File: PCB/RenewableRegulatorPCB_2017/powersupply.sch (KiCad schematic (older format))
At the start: 12 parts, among them U2 LMR16006, U3 MCP1702-50

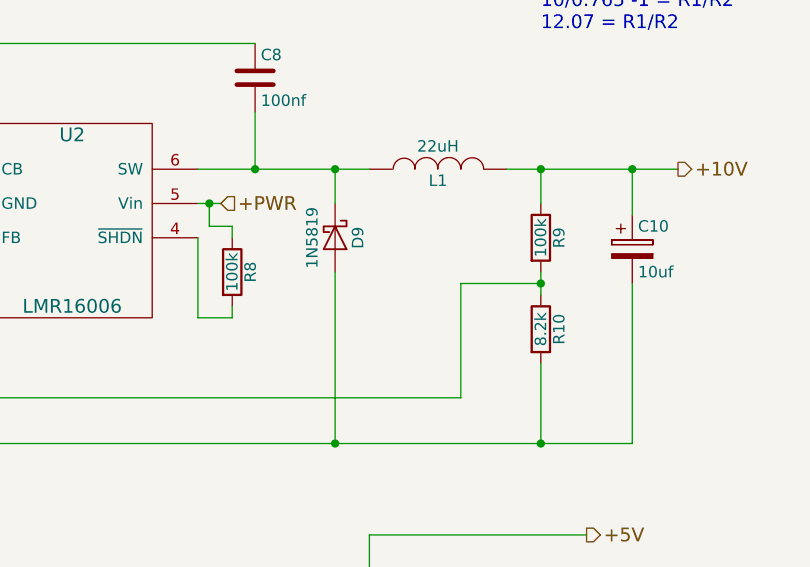
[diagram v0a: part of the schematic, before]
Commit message: Moved code into new file structure
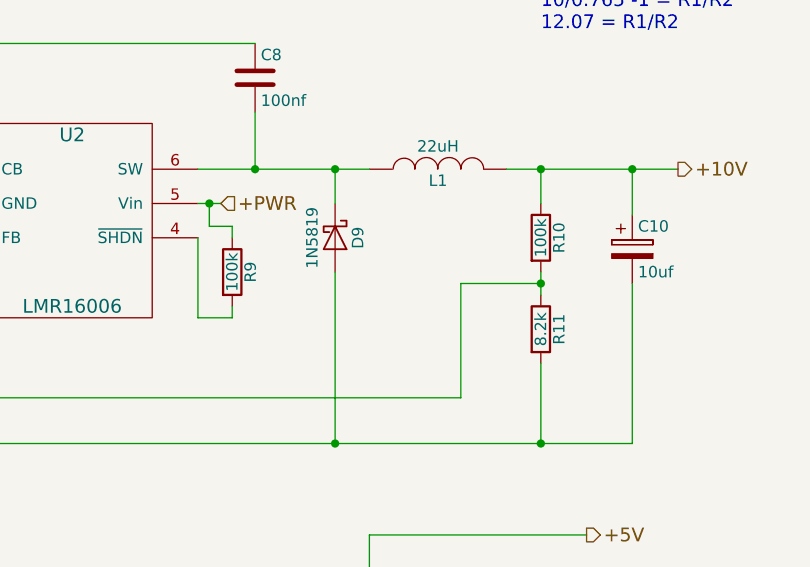
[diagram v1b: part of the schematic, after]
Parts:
- renumbered R9 to R10, R10 to R11, R8 to R9
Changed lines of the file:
@@
 $EndComp
 $Comp
-L R R9
+L R R10
 U 1 1 58E394A9
 P 6300 3500
-F 0 "R9" V 6380 3500 50  0000 C CNN
+F 0 "R10" V 6380 3500 50  0000 C CNN
 F 1 "100k" V 6300 3500 50  0000 C CNN
 F 2 "REInnovationFootprint:TH_Resistor_1" V 6230 3500 50  0001 C CNN
@@
 $EndComp
 $Comp
-L R R10
+L R R11
 U 1 1 58E394EA
 P 6300 3900
-F 0 "R10" V 6380 3900 50  0000 C CNN
+F 0 "R11" V 6380 3900 50  0000 C CNN
 F 1 "8.2k" V 6300 3900 50  0000 C CNN
 F 2 "REInnovationFootprint:TH_Resistor_1" V 6230 3900 50  0001 C CNN
@@
 VOUT = 0.765 V (1+(R1/R2))\n10/0.765 -1 = R1/R2\n12.07 = R1/R2
 $Comp
-L R R8
+L R R9
 U 1 1 58E3B2B4
 P 4950 3650
-F 0 "R8" V 5030 3650 50  0000 C CNN
+F 0 "R9" V 5030 3650 50  0000 C CNN
 F 1 "100k" V 4950 3650 50  0000 C CNN
 F 2 "REInnovationFootprint:TH_Resistor_1" V 4880 3650 50  0001 C CNN

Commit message: Large update of PCB design
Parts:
- added P11: TP_GND, matts_components:1pin_0_8mm, symbol CONN_01X01
- added P12: TP_5V, matts_components:1pin_0_8mm, symbol CONN_01X01
- added P13: TP_10V, matts_components:1pin_0_8mm, symbol CONN_01X01
- C10: Description Low ESR -> Low ESR. 25V; Manufacturer (none) -> Panasonic; Manufacturer Part No (none) -> EEUFR1H100; Supplier 1 (none) -> RS; Supplier 1 Cost (none) -> 0.047; Supplier 1 Part No (none) -> 923-2745
- C6: Description 60V+ Ceramic -> 60V+ Ceramic Low ESR; Manufacturer (none) -> Murata; Manufacturer Part No (none) -> RDEC72A225K3M1H03A; Supplier 1 (none) -> RS; Supplier 1 Cost (none) -> 0.79; Supplier 1 Part No (none) -> 133-5714
- C7, C9: Description (none) -> >25V Electrolytic/Ceramic; Manufacturer (none) -> Murata; Manufacturer Part No (none) -> RCER71H105K2M1H03A; Supplier 1 (none) -> RS; Supplier 1 Cost (none) -> 0.28; Supplier 1 Part No (none) -> 841-0755
- U2: footprint matts_components:SOT23-5_matt -> REInnovationFootprint:SM_SOT23-6
- U3: Description (none) -> LDO 5V supply. 250mA; Manufacturer (none) -> MicroChip; Manufacturer Part No (none) -> MCP1702-5002E/TO; Supplier 1 (none) -> RS; Supplier 1 Cost (none) -> 0.358; Supplier 1 Part No (none) -> 403-856
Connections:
- net +10V: now also P13.1 (P1)
- net +5V: now also P12.1 (P1)
- net GND: now also P11.1 (P1)
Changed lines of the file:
@@
 F 2 "REInnovationFootprint:C_1V7_TH" H 4400 5450 60  0001 C CNN
 F 3 "" H 4400 5450 60  0001 C CNN
+F 4 "~" H 4400 5450 60  0000 C CNN "Notes"
+F 5 ">25V Electrolytic/Ceramic" H 4400 5450 60  0001 C CNN "Description"
+F 6 "Murata" H 4400 5450 60  0001 C CNN "Manufacturer"
+F 7 "RCER71H105K2M1H03A" H 4400 5450 60  0001 C CNN "Manufacturer Part No"
+F 8 "RS" H 4400 5450 60  0001 C CNN "Supplier 1"
+F 9 "841-0755" H 4400 5450 60  0001 C CNN "Supplier 1 Part No"
+F 10 "0.28" H 4400 5450 60  0001 C CNN "Supplier 1 Cost"
+F 11 "~" H 4400 5450 60  0001 C CNN "Supplier 2"
+F 12 "~" H 4400 5450 60  0001 C CNN "Supplier 2 Part No"
+F 13 "~" H 4400 5450 60  0001 C CNN "Supplier 2 Cost"
 	1    4400 5450
-	1    0    0    -1
-$EndComp
-$Comp
-L CP1-RESCUE-RenewableRegulatorPCB_2017 C9
-U 1 1 50D36323
-P 5550 5500
-F 0 "C9" H 5600 5600 50  0000 L CNN
-F 1 "1uf" H 5600 5400 50  0000 L CNN
-F 2 "REInnovationFootprint:C_1V7_TH" H 5550 5500 60  0001 C CNN
-F 3 "" H 5550 5500 60  0001 C CNN
-	1    5550 5500
 	1    0    0    -1
 $EndComp
@@
 +5V
 Wire Wire Line
-	5550 5950 2600 5950
+	2600 5950 5750 5950
 Connection ~ 4900 5950
 Connection ~ 4400 5950
@@
 F 0 "U2" H 4250 3750 60  0000 C CNN
 F 1 "LMR16006" H 4250 3000 60  0000 C CNN
-F 2 "matts_components:SOT23-5_matt" H 4800 3500 60  0001 C CNN
+F 2 "REInnovationFootprint:SM_SOT23-6" H 4800 3500 60  0001 C CNN
 F 3 "http://www.ti.com/lit/ds/symlink/lmr16006.pdf" H 4800 3500 60  0001 C CNN
 F 4 "~" H 4250 3400 60  0000 C CNN "Notes"
@@
 F 1 "2.2uf" H 2875 3100 50  0000 L CNN
 F 2 "REInnovationFootprint:C_1V7_TH" H 2888 3050 50  0001 C CNN
-F 3 "" H 2850 3200 50  0000 C CNN
+F 3 "http://docs-europe.electrocomponents.com/webdocs/156e/0900766b8156ecdd.pdf" H 2850 3200 50  0001 C CNN
 F 4 "~" H 2850 3200 60  0000 C CNN "Notes"
-F 5 "60V+ Ceramic" H 2850 3200 60  0001 C CNN "Description"
-F 6 "~" H 2850 3200 60  0001 C CNN "Manufacturer"
-F 7 "~" H 2850 3200 60  0001 C CNN "Manufacturer Part No"
-F 8 "~" H 2850 3200 60  0001 C CNN "Supplier 1"
-F 9 "~" H 2850 3200 60  0001 C CNN "Supplier 1 Part No"
-F 10 "~" H 2850 3200 60  0001 C CNN "Supplier 1 Cost"
+F 5 "60V+ Ceramic Low ESR" H 2850 3200 60  0001 C CNN "Description"
+F 6 "Murata" H 2850 3200 60  0001 C CNN "Manufacturer"
+F 7 "RDEC72A225K3M1H03A" H 2850 3200 60  0001 C CNN "Manufacturer Part No"
+F 8 "RS" H 2850 3200 60  0001 C CNN "Supplier 1"
+F 9 "133-5714" H 2850 3200 60  0001 C CNN "Supplier 1 Part No"
+F 10 "0.79" H 2850 3200 60  0001 C CNN "Supplier 1 Cost"
 F 11 "~" H 2850 3200 60  0001 C CNN "Supplier 2"
 F 12 "~" H 2850 3200 60  0001 C CNN "Supplier 2 Part No"
@@
 F 3 "http://docs-europe.electrocomponents.com/webdocs/0a77/0900766b80a77df4.pdf" H 4900 5250 60  0001 C CNN
 F 4 "~" H 4900 5250 60  0000 C CNN "Notes"
-F 5 "~" H 4900 5250 60  0001 C CNN "Description"
-F 6 "~" H 4900 5250 60  0001 C CNN "Manufacturer"
-F 7 "~" H 4900 5250 60  0001 C CNN "Manufacturer Part No"
-F 8 "~" H 4900 5250 60  0001 C CNN "Supplier 1"
-F 9 "~" H 4900 5250 60  0001 C CNN "Supplier 1 Part No"
-F 10 "~" H 4900 5250 60  0001 C CNN "Supplier 1 Cost"
+F 5 "LDO 5V supply. 250mA" H 4900 5250 60  0001 C CNN "Description"
+F 6 "MicroChip" H 4900 5250 60  0001 C CNN "Manufacturer"
+F 7 "MCP1702-5002E/TO" H 4900 5250 60  0001 C CNN "Manufacturer Part No"
+F 8 "RS" H 4900 5250 60  0001 C CNN "Supplier 1"
+F 9 "403-856" H 4900 5250 60  0001 C CNN "Supplier 1 Part No"
+F 10 "0.358" H 4900 5250 60  0001 C CNN "Supplier 1 Cost"
 F 11 "~" H 4900 5250 60  0001 C CNN "Supplier 2"
 F 12 "~" H 4900 5250 60  0001 C CNN "Supplier 2 Part No"
@@
 F 3 "" H 6700 3550 50  0000 C CNN
 F 4 "~" H 6700 3550 60  0000 C CNN "Notes"
-F 5 "Low ESR" H 6700 3550 60  0001 C CNN "Description"
-F 6 "~" H 6700 3550 60  0001 C CNN "Manufacturer"
-F 7 "~" H 6700 3550 60  0001 C CNN "Manufacturer Part No"
-F 8 "~" H 6700 3550 60  0001 C CNN "Supplier 1"
-F 9 "~" H 6700 3550 60  0001 C CNN "Supplier 1 Part No"
-F 10 "~" H 6700 3550 60  0001 C CNN "Supplier 1 Cost"
+F 5 "Low ESR. 25V" H 6700 3550 60  0001 C CNN "Description"
+F 6 "Panasonic" H 6700 3550 60  0001 C CNN "Manufacturer"
+F 7 "EEUFR1H100" H 6700 3550 60  0001 C CNN "Manufacturer Part No"
+F 8 "RS" H 6700 3550 60  0001 C CNN "Supplier 1"
+F 9 "923-2745" H 6700 3550 60  0001 C CNN "Supplier 1 Part No"
+F 10 "0.047" H 6700 3550 60  0001 C CNN "Supplier 1 Cost"
 F 11 "~" H 6700 3550 60  0001 C CNN "Supplier 2"
 F 12 "~" H 6700 3550 60  0001 C CNN "Supplier 2 Part No"
@@
 Wire Wire Line
 	2850 2900 2650 2900
+$Comp
+L CONN_01X01 P13
+U 1 1 58E51FB7
+P 6750 2950
+F 0 "P13" H 6750 3050 50  0000 C CNN
+F 1 "TP_10V" V 6850 2950 50  0000 C CNN
+F 2 "matts_components:1pin_0_8mm" H 6750 2950 50  0001 C CNN
+F 3 "" H 6750 2950 50  0000 C CNN
+	1    6750 2950
+	1    0    0    -1
+$EndComp
+$Comp
+L CONN_01X01 P12
+U 1 1 58E5205A
+P 6300 5050
+F 0 "P12" H 6300 5150 50  0000 C CNN
+F 1 "TP_5V" V 6400 5050 50  0000 C CNN
+F 2 "matts_components:1pin_0_8mm" H 6300 5050 50  0001 C CNN
+F 3 "" H 6300 5050 50  0000 C CNN
+	1    6300 5050
+	1    0    0    -1
+$EndComp
+$Comp
+L CONN_01X01 P11
+U 1 1 58E520E9
+P 5950 5950
+F 0 "P11" H 5950 6050 50  0000 C CNN
+F 1 "TP_GND" V 6050 5950 50  0000 C CNN
+F 2 "matts_components:1pin_0_8mm" H 5950 5950 50  0001 C CNN
+F 3 "" H 5950 5950 50  0000 C CNN
+	1    5950 5950
+	1    0    0    -1
+$EndComp
+Wire Wire Line
+	6550 2950 6450 2950
+Wire Wire Line
+	6450 2950 6450 3200
+Connection ~ 6450 3200
+Wire Wire Line
+	6100 5050 5950 5050
+Wire Wire Line
+	5950 5050 5950 4800
+Connection ~ 5950 4800
+Connection ~ 5550 5950
+$Comp
+L CP1-RESCUE-RenewableRegulatorPCB_2017 C9
+U 1 1 58E5783F
+P 5550 5500
+F 0 "C9" H 5600 5600 50  0000 L CNN
+F 1 "1uf" H 5600 5400 50  0000 L CNN
+F 2 "REInnovationFootprint:C_1V7_TH" H 5550 5500 60  0001 C CNN
+F 3 "" H 5550 5500 60  0001 C CNN
+F 4 "~" H 5550 5500 60  0000 C CNN "Notes"
+F 5 ">25V Electrolytic/Ceramic" H 5550 5500 60  0001 C CNN "Description"
+F 6 "Murata" H 5550 5500 60  0001 C CNN "Manufacturer"
+F 7 "RCER71H105K2M1H03A" H 5550 5500 60  0001 C CNN "Manufacturer Part No"
+F 8 "RS" H 5550 5500 60  0001 C CNN "Supplier 1"
+F 9 "841-0755" H 5550 5500 60  0001 C CNN "Supplier 1 Part No"
+F 10 "0.28" H 5550 5500 60  0001 C CNN "Supplier 1 Cost"
+F 11 "~" H 5550 5500 60  0001 C CNN "Supplier 2"
+F 12 "~" H 5550 5500 60  0001 C CNN "Supplier 2 Part No"
+F 13 "~" H 5550 5500 60  0001 C CNN "Supplier 2 Cost"
+	1    5550 5500
+	1    0    0    -1
+$EndComp
 $EndSCHEMATC

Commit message: Secod
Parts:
- C10: footprint REInnovationFootprint:C_1V7_TH -> RenewableRegulatorPCB_2017_Library_Yoan:Capacitor_C10_1V7_TH
- C6: footprint REInnovationFootprint:C_1V7_TH -> RenewableRegulatorPCB_2017_Library_Yoan:Capacitor_C6_1V7_TH
- C7: footprint REInnovationFootprint:C_1V7_TH -> RenewableRegulatorPCB_2017_Library_Yoan:Capacitor_C7_1V7_TH
- C9: footprint REInnovationFootprint:C_1V7_TH -> RenewableRegulatorPCB_2017_Library_Yoan:Capacitor_C9_1V7_TH
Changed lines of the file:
@@
 LIBS:device
 LIBS:conn
+LIBS:RenewableRegulatorPCB_2017
 LIBS:RenewableRegulatorPCB_2017-cache
 EELAYER 25 0
@@
 F 0 "C7" H 4450 5550 50  0000 L CNN
 F 1 "1uf" H 4450 5350 50  0000 L CNN
-F 2 "REInnovationFootprint:C_1V7_TH" H 4400 5450 60  0001 C CNN
-F 3 "" H 4400 5450 60  0001 C CNN
+F 2 "RenewableRegulatorPCB_2017_Library_Yoan:Capacitor_C7_1V7_TH" H 4400 5450 60  0001 C CNN
+F 3 "" H 4400 5450 210 0001 C CNN
 F 4 "~" H 4400 5450 60  0000 C CNN "Notes"
 F 5 ">25V Electrolytic/Ceramic" H 4400 5450 60  0001 C CNN "Description"
 F 6 "Murata" H 4400 5450 60  0001 C CNN "Manufacturer"
-F 7 "RCER71H105K2M1H03A" H 4400 5450 60  0001 C CNN "Manufacturer Part No"
+F 7 "RCER71H105K2M1H03A" H 4400 5450 200 0001 C CNN "Manufacturer Part No"
 F 8 "RS" H 4400 5450 60  0001 C CNN "Supplier 1"
 F 9 "841-0755" H 4400 5450 60  0001 C CNN "Supplier 1 Part No"
@@
 F 0 "C6" H 2875 3300 50  0000 L CNN
 F 1 "2.2uf" H 2875 3100 50  0000 L CNN
-F 2 "REInnovationFootprint:C_1V7_TH" H 2888 3050 50  0001 C CNN
-F 3 "http://docs-europe.electrocomponents.com/webdocs/156e/0900766b8156ecdd.pdf" H 2850 3200 50  0001 C CNN
+F 2 "RenewableRegulatorPCB_2017_Library_Yoan:Capacitor_C6_1V7_TH" H 2888 3050 50  0001 C CNN
+F 3 "http://docs-europe.electrocomponents.com/webdocs/156e/0900766b8156ecdd.pdf" H 2850 3200 210 0001 C CNN
 F 4 "~" H 2850 3200 60  0000 C CNN "Notes"
 F 5 "60V+ Ceramic Low ESR" H 2850 3200 60  0001 C CNN "Description"
 F 6 "Murata" H 2850 3200 60  0001 C CNN "Manufacturer"
-F 7 "RDEC72A225K3M1H03A" H 2850 3200 60  0001 C CNN "Manufacturer Part No"
+F 7 "RDEC72A225K3M1H03A" H 2850 3200 200 0001 C CNN "Manufacturer Part No"
 F 8 "RS" H 2850 3200 60  0001 C CNN "Supplier 1"
 F 9 "133-5714" H 2850 3200 60  0001 C CNN "Supplier 1 Part No"
@@
 F 0 "C10" H 6725 3650 50  0000 L CNN
 F 1 "10uf" H 6725 3450 50  0000 L CNN
-F 2 "REInnovationFootprint:C_1V7_TH" H 6738 3400 50  0001 C CNN
-F 3 "" H 6700 3550 50  0000 C CNN
+F 2 "RenewableRegulatorPCB_2017_Library_Yoan:Capacitor_C10_1V7_TH" H 6738 3400 50  0001 C CNN
+F 3 "" H 6700 3550 200 0000 C CNN
 F 4 "~" H 6700 3550 60  0000 C CNN "Notes"
 F 5 "Low ESR. 25V" H 6700 3550 60  0001 C CNN "Description"
 F 6 "Panasonic" H 6700 3550 60  0001 C CNN "Manufacturer"
-F 7 "EEUFR1H100" H 6700 3550 60  0001 C CNN "Manufacturer Part No"
+F 7 "EEUFR1H100" H 6700 3550 200 0001 C CNN "Manufacturer Part No"
 F 8 "RS" H 6700 3550 60  0001 C CNN "Supplier 1"
 F 9 "923-2745" H 6700 3550 60  0001 C CNN "Supplier 1 Part No"
@@
 F 0 "C9" H 5600 5600 50  0000 L CNN
 F 1 "1uf" H 5600 5400 50  0000 L CNN
-F 2 "REInnovationFootprint:C_1V7_TH" H 5550 5500 60  0001 C CNN
-F 3 "" H 5550 5500 60  0001 C CNN
+F 2 "RenewableRegulatorPCB_2017_Library_Yoan:Capacitor_C9_1V7_TH" H 5550 5500 60  0001 C CNN
+F 3 "" H 5550 5500 210 0001 C CNN
 F 4 "~" H 5550 5500 60  0000 C CNN "Notes"
 F 5 ">25V Electrolytic/Ceramic" H 5550 5500 60  0001 C CNN "Description"
 F 6 "Murata" H 5550 5500 60  0001 C CNN "Manufacturer"
-F 7 "RCER71H105K2M1H03A" H 5550 5500 60  0001 C CNN "Manufacturer Part No"
+F 7 "RCER71H105K2M1H03A" H 5550 5500 200 0001 C CNN "Manufacturer Part No"
 F 8 "RS" H 5550 5500 60  0001 C CNN "Supplier 1"
 F 9 "841-0755" H 5550 5500 60  0001 C CNN "Supplier 1 Part No"

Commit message: Last version of regulator PCB
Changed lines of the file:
@@
 LIBS:power
 LIBS:device
+LIBS:matts_components
 LIBS:conn
 LIBS:RenewableRegulatorPCB_2017
-LIBS:matts_components
 LIBS:RenewableRegulatorPCB_2017-cache
 EELAYER 25 0
@@
 	4400 5250 4400 5200
 Connection ~ 4400 5200
-Text Notes 6300 2600 0    60   ~ 0
+Text Notes 6750 1750 0    60   ~ 0
 VOUT = 0.765 V (1+(R1/R2))\n10/0.765 -1 = R1/R2\n12.07 = R1/R2
 $Comp
